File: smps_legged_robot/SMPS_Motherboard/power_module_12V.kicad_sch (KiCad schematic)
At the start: 2 parts, among them J3 PESC-02-12-02-01-X-VT-LC

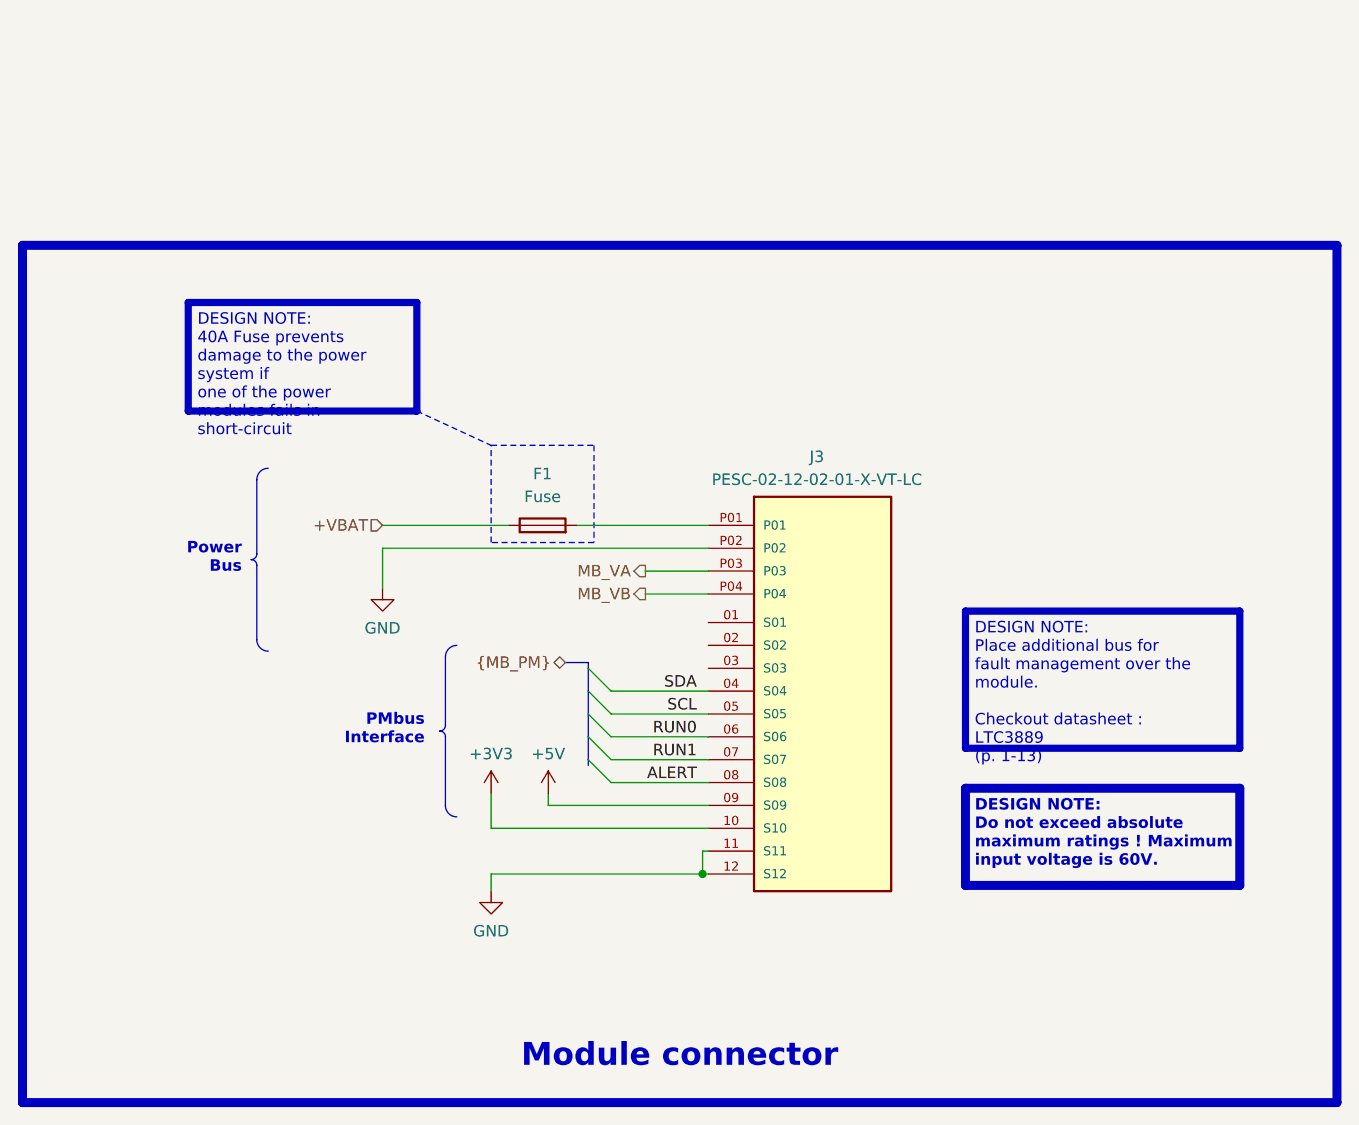
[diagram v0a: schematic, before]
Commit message: Buck module finished pending review
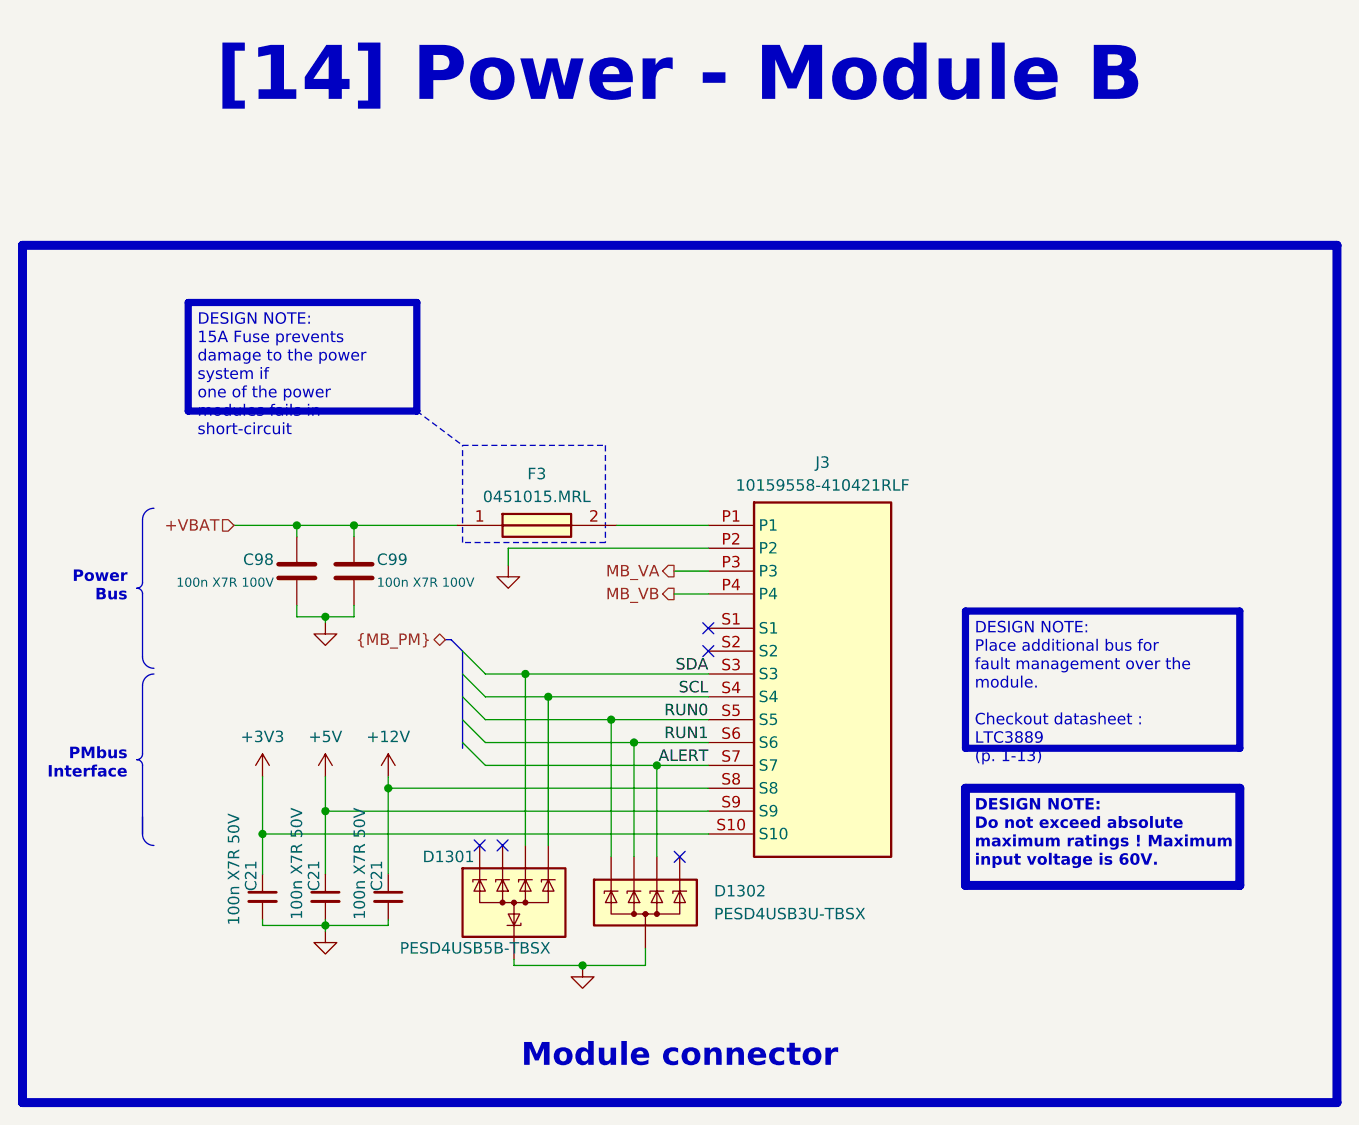
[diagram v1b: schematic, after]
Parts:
- removed F1: Fuse, symbol Device:Fuse
- removed J3: PESC-02-12-02-01-X-VT-LC, PESC-02-12-02-01-X-VT-LC:SAMTEC_PESC-02-12-02-01-X-VT-LC, symbol PESC-02-12-02-01-X-VT-LC:PESC-02-12-02-01-X-VT-LC
- added C21 (x3): 100n X7R 50V, 0_capacitor_smd:C_0402_1005_DensityHigh, symbol Device:C_Small
- added C98, C99: 100n X7R 100V, 0_capacitor_smd:C_0603_1608_DensityHigh, symbol Device:C
- added D1301: PESD4USB5B-TBSX, 0_package_DFN_QFN:SOT1176D, symbol 0_power_protection:PESD4USB5B-TBSX
- added D1302: PESD4USB3U-TBSX, 0_package_DFN_QFN:SOT1176D, symbol 0_power_protection:PESD4USB3U-TBSX
- added F3: 0451015.MRL, 0_diode_smd:FUSC6127X294N, symbol 0451015_MRL:0451015.MRL
- added J3: 10159558-410421RLF, 0_connectors:10159558410421RLF, symbol 10159558-410421RLF:10159558-410421RLF
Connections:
- net +3V3: now also C21.1, J3.S10
- net +5V: now also C21.1, J3.S9
- net +VBAT: now also C98.1, C99.1, F3.1
- net ALERT: now also D1302.4 (K), D1302.7 (K), J3.S7
- net GND: now also C21.2, C21.2, C21.2, C98.2, C99.2, D1301.3 (A), D1301.8 (A), D1302.3 (A), D1302.8 (A), J3.P2
- net RUN0: now also D1302.1 (K), D1302.10 (K), J3.S5
- net RUN1: now also D1302.2 (K), D1302.9 (K), J3.S6
- net SCL: now also D1301.5 (K), D1301.6 (K), J3.S4
- net SDA: now also D1301.4 (K), D1301.7 (K), J3.S3
- new net: F3.2, J3.P1
- new net: D1301.1 (K), D1301.10 (K)
- new net: D1301.2 (K), D1301.9 (K)
- new net: D1302.5 (K), D1302.6 (K)
- new net +12V: C21.1, J3.S8
- new net MB_VA: J3.P3
- new net MB_VB: J3.P4
- no-connect marks 0 -> 5
